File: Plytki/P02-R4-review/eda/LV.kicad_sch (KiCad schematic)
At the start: 18 parts, among them J10 LV10, J3 LV03, J4 LV04, J5 LV05, J6 LV06, J7 LV07, J8 LV08, J9 LV09, U5 TSR 2-2450, U6 TSR 2-2433

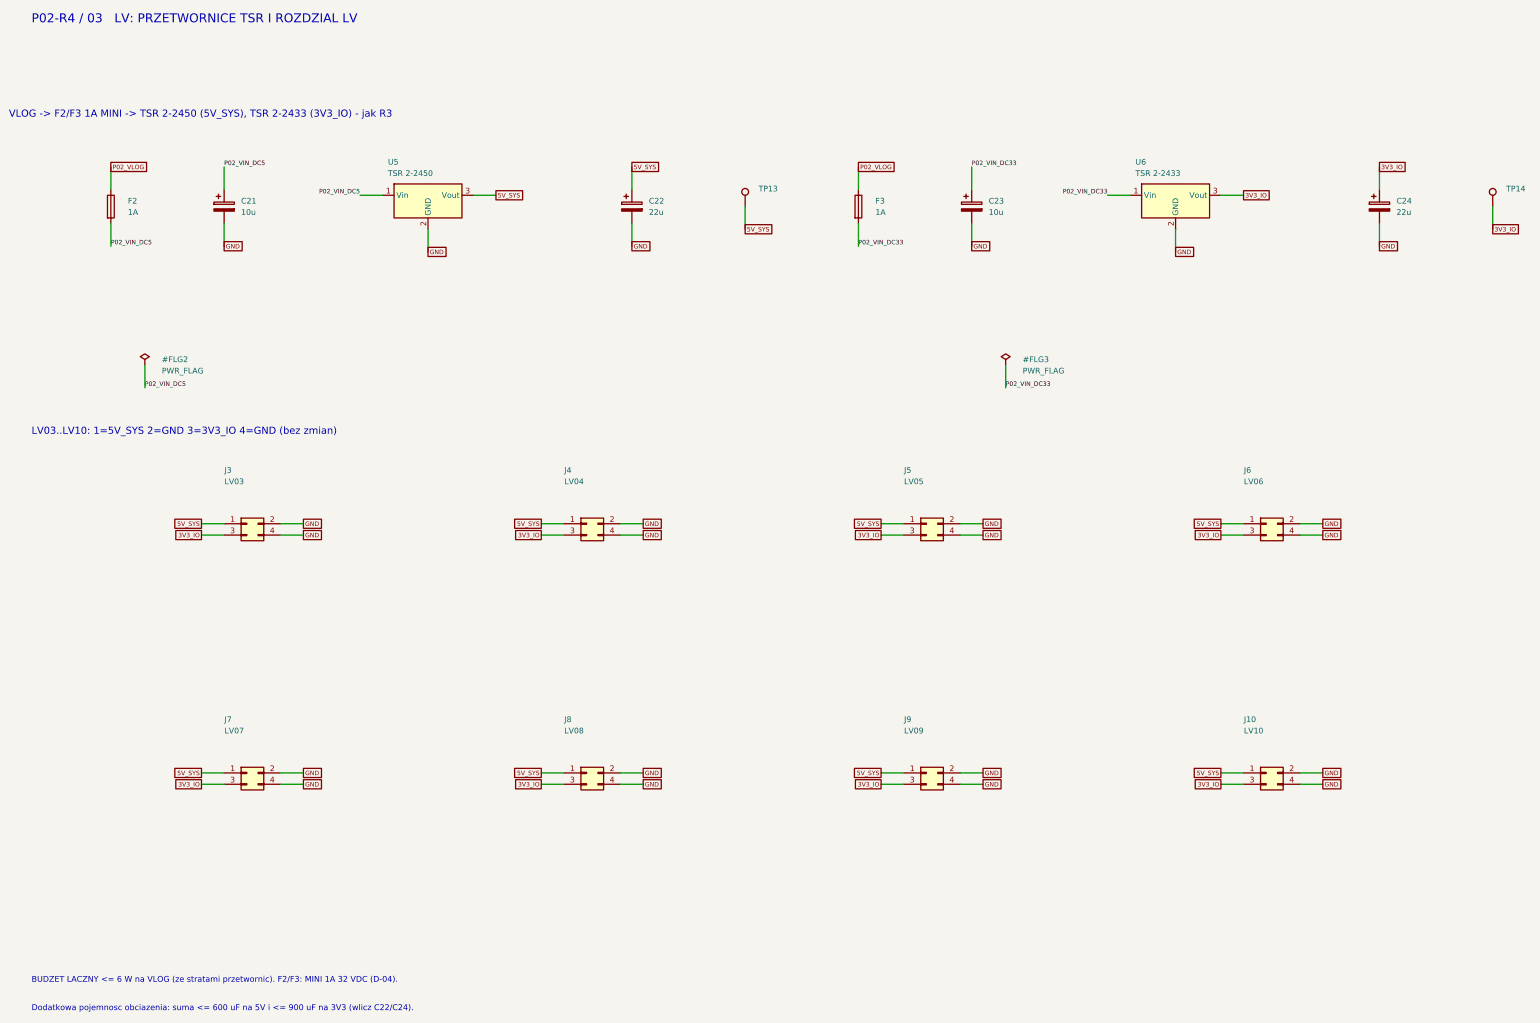
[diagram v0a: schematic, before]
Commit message: P02 R4 etap 2: schemat w formacie S1
- D3 5KP24A (R4E1-01), kontrola Z-01 (T15) z proba ujemna 5KP18A
- J_BP (IDC 2x10, pinout S1 par. 8) zamiast J3-J13 i J16; kontrola T16
- listwy serwisowe J_SV1/J_SV2 z rezystorami szeregowymi R50-R71 (S1 par. 6); T17, L05
- TP1-TP17 usuniete (punkty na listwach); J15: bezpiecznik 1 A (R4E1-06)
- rezystory THT z zakupow P01 na stojaco, nowe SMD 1206; U9 SOIC-14 bez adaptera
- C_H lezacy (wlasny footprint), wysokosci w parts.py
- ERC 0, 342/342 pinow, kontrole elektryczne 39/39, proby ujemne 25/25

Co-Authored-By: Claude Opus 5.5 <noreply@anthropic.com>
Claude-Session: https://claude.ai/code/session_017A5ySSfWiiFz2upyoitzhg
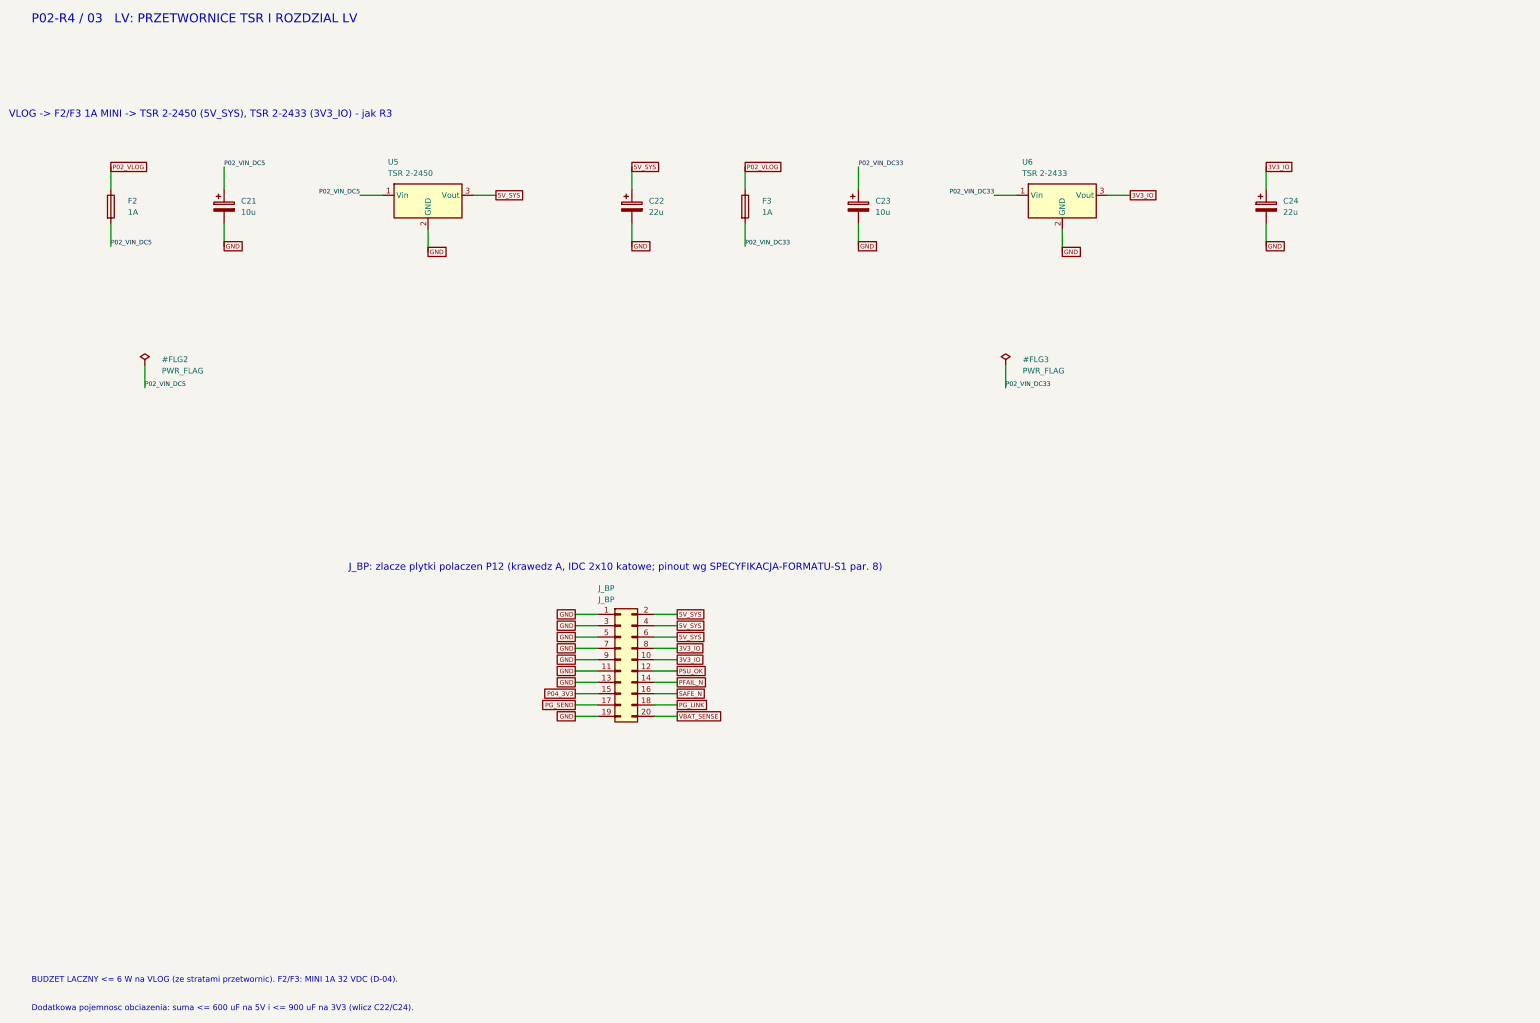
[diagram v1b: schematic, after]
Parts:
- removed J10: LV10, Connector_Molex:Molex_Mini-Fit_Jr_5566-04A_2x02_P4.20mm_Vertical, symbol P02:Conn_02x02_Odd_Even
- removed J3: LV03, Connector_Molex:Molex_Mini-Fit_Jr_5566-04A_2x02_P4.20mm_Vertical, symbol P02:Conn_02x02_Odd_Even
- removed J4: LV04, Connector_Molex:Molex_Mini-Fit_Jr_5566-04A_2x02_P4.20mm_Vertical, symbol P02:Conn_02x02_Odd_Even
- removed J5: LV05, Connector_Molex:Molex_Mini-Fit_Jr_5566-04A_2x02_P4.20mm_Vertical, symbol P02:Conn_02x02_Odd_Even
- removed J6: LV06, Connector_Molex:Molex_Mini-Fit_Jr_5566-04A_2x02_P4.20mm_Vertical, symbol P02:Conn_02x02_Odd_Even
- removed J7: LV07, Connector_Molex:Molex_Mini-Fit_Jr_5566-04A_2x02_P4.20mm_Vertical, symbol P02:Conn_02x02_Odd_Even
- removed J8: LV08, Connector_Molex:Molex_Mini-Fit_Jr_5566-04A_2x02_P4.20mm_Vertical, symbol P02:Conn_02x02_Odd_Even
- removed J9: LV09, Connector_Molex:Molex_Mini-Fit_Jr_5566-04A_2x02_P4.20mm_Vertical, symbol P02:Conn_02x02_Odd_Even
- removed TP13, TP14: (no value), P02:TestPad_1, symbol P02:TestPoint
- added J_BP: J_BP, Connector_IDC:IDC-Header_2x10_P2.54mm_Horizontal, symbol P02:Conn_02x10_Odd_Even
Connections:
- net 3V3_IO: now also J_BP.10 (Pin_10), J_BP.8 (Pin_8)
- net 5V_SYS: now also J_BP.2 (Pin_2), J_BP.4 (Pin_4), J_BP.6 (Pin_6)
- net GND: now also J_BP.1 (Pin_1), J_BP.11 (Pin_11), J_BP.13 (Pin_13), J_BP.19 (Pin_19), J_BP.3 (Pin_3), J_BP.5 (Pin_5), J_BP.7 (Pin_7), J_BP.9 (Pin_9)
- new net P04_3V3: J_BP.15 (Pin_15)
- new net PFAIL_N: J_BP.14 (Pin_14)
- new net PG_LINK: J_BP.18 (Pin_18)
- new net PG_SEND: J_BP.17 (Pin_17)
- new net PSU_OK: J_BP.12 (Pin_12)
- new net SAFE_N: J_BP.16 (Pin_16)
- new net VBAT_SENSE: J_BP.20 (Pin_20)
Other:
- note added: "J_BP: zlacze plytki polaczen P12 (krawedz A, IDC 2x10 katowe; pinout wg SPECYFIKACJA-FORMATU-S1 par. 8)"
- note removed: "LV03..LV10: 1=5V_SYS 2=GND 3=3V3_IO 4=GND (bez zmian)"
- company: EGRLab / schematic review (etap 1, bez PCB) -> EGRLab / etap 2: format S1 (plytka 2/3, sloty S2-S3)
- moved on the sheet: C23, C24, F3, U6
